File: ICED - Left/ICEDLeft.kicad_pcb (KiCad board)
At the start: 2 copper layers, 175.4 x 145 mm, 164 parts, among them P1 FLASH_HDR, P2 USBC, P3 CONN_17, P4 USB3_AFEMALE, Q1 TC1264, U1 MK20DX256VLH7, U2 IS31FL3731C, X1 CRYSTAL

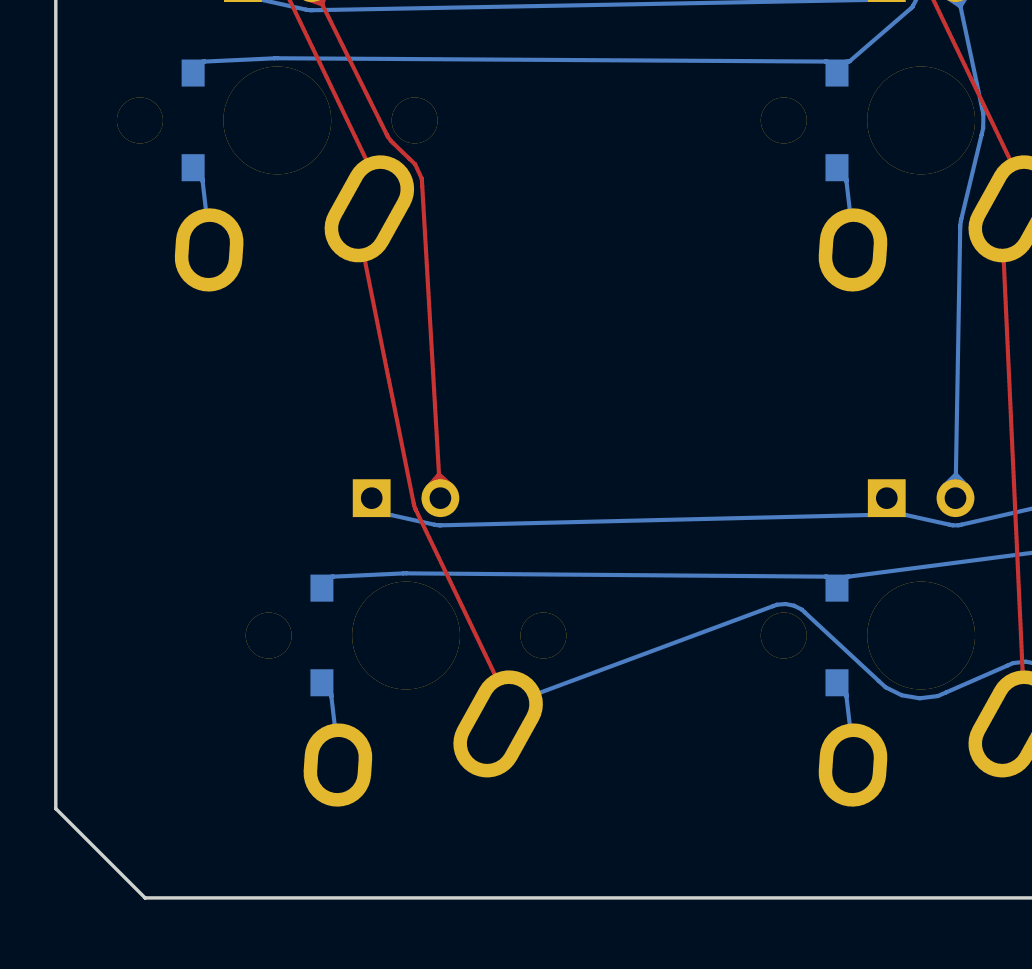
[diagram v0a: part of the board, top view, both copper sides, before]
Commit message: moved S38
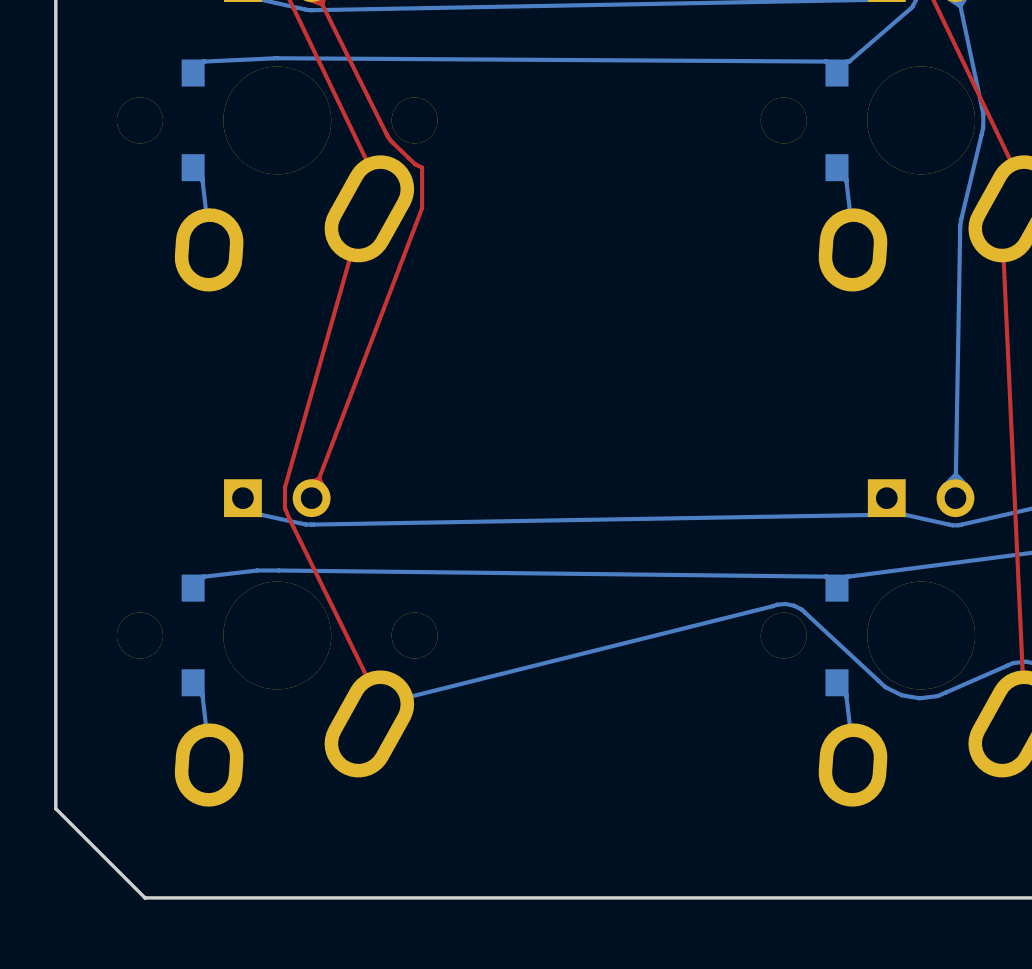
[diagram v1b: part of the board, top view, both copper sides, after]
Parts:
- moved D38 4.76 mm to (22.7, 125.8)
- moved D76 4.76 mm to (25.8, 120.7)
- moved S38 4.76 mm to (25.8, 125.8)
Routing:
- net /Row5: track 194.4 -> 199.2 mm
- net /ledmatrix/CA9: track 101.9 -> 106.6 mm
- net /Col9: track 190.3 -> 195.0 mm
- net /ledmatrix/CA4: track 288.6 -> 289.6 mm
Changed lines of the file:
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@@
   )
   (module prettylib:INSW_LEDS_REG (layer Front)
-    (at 30.607 120.724)
+    (at 25.845 120.724)
     (attr smd)
     (fp_text reference D76 (at 0 -1.5) (layer B.SilkS)
@@
   )
   (module prettylib:SOT123-DIODE (layer Back)
-    (at 27.4955 125.804 180)
+    (at 22.7335 125.804 180)
     (descr DIODE)
     (tags DIODE)
@@
   )
   (module prettylib:MXALPS (layer Front)
-    (at 30.607 125.804 180)
+    (at 25.845 125.804 180)
     (descr MXALPS)
     (tags MXALPS)
@@
   (segment (start 127.3566 89.4242) (end 127.3368 89.5061) (width 0.1524) (layer Front) (net 5))
   (segment (start 127.127 99.769) (end 127.3136 89.7594) (width 0.1524) (layer Front) (net 5))
-  (segment (start 31.2071 109.2034) (end 31.877 120.724) (width 0.1524) (layer Front) (net 5))
+  (segment (start 27.4 120) (end 27.7 120.6) (width 0.1524) (layer Front) (net 5))
+  (segment (start 27.4 120) (end 26.6493 120.31777) (width 0.1524) (layer Front) (net 5))
+  (segment (start 31.2 110) (end 27.115 120.724) (width 0.1524) (layer Front) (net 5))
+  (segment (start 31.2 110) (end 31.2 108.5) (width 0.1524) (layer Front) (net 5))
+  (segment (start 31.2 108.5) (end 30.9442 108.3764) (width 0.1524) (layer Front) (net 5))
   (segment (start 30.9442 108.3764) (end 30.733 108.1734) (width 0.1524) (layer Front) (net 5))
-  (segment (start 31.19 108.9101) (end 30.9442 108.3764) (width 0.1524) (layer Front) (net 5))
-  (segment (start 31.2071 109.2034) (end 31.19 108.9101) (width 0.1524) (layer Front) (net 5))
   (segment (start 30.1235 107.5868) (end 30.733 108.1734) (width 0.1524) (layer Front) (net 5))
   (segment (start 30.0519 107.5179) (end 30.1235 107.5868) (width 0.1524) (layer Front) (net 5))
@@
   (segment (start 127.1435 98.8863) (end 127.5764 99.3447) (width 0.1524) (layer Front) (net 5))
   (segment (start 127.1435 98.8863) (end 126.6938 99.3283) (width 0.1524) (layer Front) (net 5))
-  (segment (start 31.8257 119.8426) (end 32.2925 120.2665) (width 0.1524) (layer Front) (net 5))
-  (segment (start 31.8257 119.8426) (end 31.4113 120.3177) (width 0.1524) (layer Front) (net 5))
   (segment (start 27.5073 102.4649) (end 26.9118 102.2576) (width 0.1524) (layer Front) (net 5))
   (segment (start 27.5073 102.4649) (end 27.7026 101.8654) (width 0.1524) (layer Front) (net 5))
@@
   (segment (start 125.0762 115.6598) (end 125 115.6598) (width 0.1524) (layer Back) (net 10))
   (segment (start 125.715 115.536) (end 125.0762 115.6598) (width 0.1524) (layer Back) (net 10))
-  (segment (start 29.9608 121.3478) (end 29.337 120.724) (width 0.1524) (layer Back) (net 10))
-  (segment (start 30.037 121.3478) (end 29.9608 121.3478) (width 0.1524) (layer Back) (net 10))
-  (segment (start 30.0411 121.3478) (end 30.037 121.3478) (width 0.1524) (layer Back) (net 10))
-  (segment (start 30.0495 121.3487) (end 30.0411 121.3478) (width 0.1524) (layer Back) (net 10))
-  (segment (start 30.0535 121.3496) (end 30.0495 121.3487) (width 0.1524) (layer Back) (net 10))
-  (segment (start 31.6598 121.7052) (end 30.0535 121.3496) (width 0.1524) (layer Back) (net 10))
-  (segment (start 31.8404 121.7301) (end 31.9012 121.7286) (width 0.1524) (layer Back) (net 10))
-  (segment (start 31.7198 121.7184) (end 31.8404 121.7301) (width 0.1524) (layer Back) (net 10))
-  (segment (start 31.6598 121.7052) (end 31.7198 121.7184) (width 0.1524) (layer Back) (net 10))
-  (segment (start 47.6852 121.3478) (end 31.9012 121.7286) (width 0.1524) (layer Back) (net 10))
+  (segment (start 25.1988 121.3478) (end 24.5750 120.72404) (width 0.1524) (layer Back) (net 10))
+  (segment (start 25.2750 121.3478) (end 25.1988 121.34788) (width 0.1524) (layer Back) (net 10))
+  (segment (start 25.2791 121.3478) (end 25.2750 121.34788) (width 0.1524) (layer Back) (net 10))
+  (segment (start 25.2875 121.3487) (end 25.2791 121.34788) (width 0.1524) (layer Back) (net 10))
+  (segment (start 25.2915 121.3496) (end 25.2875 121.34877) (width 0.1524) (layer Back) (net 10))
+  (segment (start 26.9 121.7) (end 25.2915 121.34966) (width 0.1524) (layer Back) (net 10))
+  (segment (start 27.1 121.7) (end 27.2 121.7) (width 0.1524) (layer Back) (net 10))
+  (segment (start 26.9 121.7) (end 27.1 121.7) (width 0.1524) (layer Back) (net 10))
+  (segment (start 47.6852 121.3478) (end 27.2 121.7) (width 0.1524) (layer Back) (net 10))
   (segment (start 47.687 121.3478) (end 47.6852 121.3478) (width 0.1524) (layer Back) (net 10))
   (segment (start 47.7632 121.3478) (end 47.687 121.3478) (width 0.1524) (layer Back) (net 10))
@@
   (segment (start 47.1572 130.3047) (end 46.8953 128.0607) (width 0.1524) (layer Back) (net 85))
   (segment (start 47.137 130.594) (end 47.1572 130.3047) (width 0.1524) (layer Back) (net 85))
-  (segment (start 27.8448 127.9757) (end 27.4955 127.5515) (width 0.1524) (layer Back) (net 86))
-  (segment (start 27.8448 128.0519) (end 27.8448 127.9757) (width 0.1524) (layer Back) (net 86))
-  (segment (start 27.8453 128.0607) (end 27.8448 128.0519) (width 0.1524) (layer Back) (net 86))
-  (segment (start 28.1072 130.3047) (end 27.8453 128.0607) (width 0.1524) (layer Back) (net 86))
-  (segment (start 28.087 130.594) (end 28.1072 130.3047) (width 0.1524) (layer Back) (net 86))
+  (segment (start 23.0828 127.9757) (end 22.7335 127.55155) (width 0.1524) (layer Back) (net 86))
+  (segment (start 23.0828 128.0519) (end 23.0828 127.97577) (width 0.1524) (layer Back) (net 86))
+  (segment (start 23.0833 128.0607) (end 23.0828 128.05199) (width 0.1524) (layer Back) (net 86))
+  (segment (start 23.3452 130.3047) (end 23.0833 128.06077) (width 0.1524) (layer Back) (net 86))
+  (segment (start 23.3250 130.5940) (end 23.3452 130.30477) (width 0.1524) (layer Back) (net 86))
   (via (at 134.545 124.816) (size 0.4064) (layers Front Back) (net 87))
   (via (at 145.642 120.711) (size 0.4064) (layers Front Back) (net 87))
@@
   (segment (start 46.12 123.6272) (end 46.1962 123.6272) (width 0.1524) (layer Back) (net 101))
   (segment (start 46.1194 123.6272) (end 46.12 123.6272) (width 0.1524) (layer Back) (net 101))
-  (segment (start 30.6251 123.5053) (end 46.1194 123.6272) (width 0.1524) (layer Back) (net 101))
-  (segment (start 30.6251 123.5053) (end 30.5005 123.5077) (width 0.1524) (layer Back) (net 101))
-  (segment (start 27.9245 123.6271) (end 30.5005 123.5077) (width 0.1524) (layer Back) (net 101))
-  (segment (start 27.921 123.6272) (end 27.9245 123.6271) (width 0.1524) (layer Back) (net 101))
-  (segment (start 27.8448 123.6272) (end 27.921 123.6272) (width 0.1524) (layer Back) (net 101))
-  (segment (start 27.4955 124.0514) (end 27.8448 123.6272) (width 0.1524) (layer Back) (net 101))
+  (segment (start 25.9 123.4) (end 46.1194 123.6272) (width 0.1524) (layer Back) (net 101))
+  (segment (start 25.9 123.4) (end 25.1 123.4) (width 0.1524) (layer Back) (net 101))
+  (segment (start 23.1625 123.6271) (end 25.1 123.4) (width 0.1524) (layer Back) (net 101))
+  (segment (start 23.1590 123.6272) (end 23.1625 123.62711) (width 0.1524) (layer Back) (net 101))
+  (segment (start 23.0828 123.6272) (end 23.1590 123.62722) (width 0.1524) (layer Back) (net 101))
+  (segment (start 22.7335 124.0514) (end 23.0828 123.62722) (width 0.1524) (layer Back) (net 101))
   (segment (start 84.2962 119.7026) (end 84.6455 119.2784) (width 0.1524) (layer Back) (net 101))
   (segment (start 84.22 119.7026) (end 84.2962 119.7026) (width 0.1524) (layer Back) (net 101))
@@
   (segment (start 50.1216 62.5031) (end 50.0592 62.233) (width 0.1524) (layer Front) (net 118))
   (segment (start 50.1216 62.5031) (end 50.2854 62.2796) (width 0.1524) (layer Front) (net 118))
-  (segment (start 34.4168 128.3437) (end 34.012 129.074) (width 0.1524) (layer Back) (net 119))
-  (segment (start 44.1747 124.7205) (end 34.4168 128.3437) (width 0.1524) (layer Back) (net 119))
+  (segment (start 29.6548 128.3437) (end 29.2500 129.07404) (width 0.1524) (layer Back) (net 119))
+  (segment (start 44.1747 124.7205) (end 29.6548 128.3437) (width 0.1524) (layer Back) (net 119))
   (segment (start 44.3254 124.6646) (end 44.1747 124.7205) (width 0.1524) (layer Back) (net 119))
   (segment (start 44.6451 124.6391) (end 44.3254 124.6646) (width 0.1524) (layer Back) (net 119))
@@
   (segment (start 138.3562 119.5848) (end 138.28 119.5848) (width 0.1524) (layer Back) (net 119))
   (segment (start 139.03 119.511) (end 138.3562 119.5848) (width 0.1524) (layer Back) (net 119))
-  (segment (start 34.4168 128.3437) (end 34.012 129.074) (width 0.1524) (layer Front) (net 119))
-  (segment (start 30.9709 121.1585) (end 34.4168 128.3437) (width 0.1524) (layer Front) (net 119))
-  (segment (start 30.944 121.1025) (end 30.9709 121.1585) (width 0.1524) (layer Front) (net 119))
-  (segment (start 30.9044 120.9843) (end 30.944 121.1025) (width 0.1524) (layer Front) (net 119))
-  (segment (start 30.8919 120.9223) (end 30.9044 120.9843) (width 0.1524) (layer Front) (net 119))
-  (segment (start 28.8452 110.7543) (end 30.8919 120.9223) (width 0.1524) (layer Front) (net 119))
+  (segment (start 29.6548 128.3437) (end 29.2500 129.07404) (width 0.1524) (layer Front) (net 119))
+  (segment (start 26.3 121.5) (end 29.6548 128.34377) (width 0.1524) (layer Front) (net 119))
+  (segment (start 26.13 121.1) (end 26.3 121.5) (width 0.1524) (layer Front) (net 119))
+  (segment (start 26.13 120.5343) (end 26.13 121.1) (width 0.1524) (layer Front) (net 119))
+  (segment (start 26.1299 120.3223) (end 26.13 120.53433) (width 0.1524) (layer Front) (net 119))
+  (segment (start 28.8452 110.7543) (end 26.1299 120.3223) (width 0.1524) (layer Front) (net 119))
   (segment (start 29.25 110.024) (end 28.8452 110.7543) (width 0.1524) (layer Front) (net 119))
   (segment (start 29.6548 71.1934) (end 29.25 71.9237) (width 0.1524) (layer Front) (net 119))
